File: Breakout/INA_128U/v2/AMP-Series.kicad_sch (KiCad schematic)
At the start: 1 part, among them U1 INA128

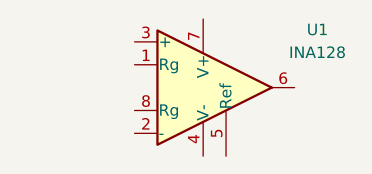
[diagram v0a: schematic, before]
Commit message: added INA128_U v2
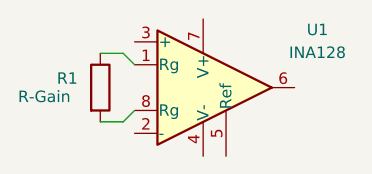
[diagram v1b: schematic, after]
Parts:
- added R1: R-Gain, symbol Device:R
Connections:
- net at U1.1 (Rg): now also R1.1
- net at U1.8 (Rg): now also R1.2
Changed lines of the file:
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@@
 	(generator_version "9.0")
 	(paper "A4")
+	(wire
+		(pts
+			(xy 25.4 43.18) (xy 27.94 43.18)
+		)
+		(stroke
+			(width 0)
+			(type default)
+		)
+	)
+	(wire
+		(pts
+			(xy 25.4 35.56) (xy 27.94 35.56)
+		)
+		(stroke
+			(width 0)
+			(type default)
+		)
+	)
+	(wire
+		(pts
+			(xy 27.94 43.18) (xy 29.21 41.91)
+		)
+		(stroke
+			(width 0)
+			(type default)
+		)
+	)
+	(wire
+		(pts
+			(xy 27.94 35.56) (xy 29.21 36.83)
+		)
+		(stroke
+			(width 0)
+			(type default)
+		)
+	)
+	(symbol
+		(lib_id "Device:R")
+		(at 25.4 39.37 0)
+		(unit 1)
+		(exclude_from_sim no)
+		(in_bom yes)
+		(on_board yes)
+		(dnp no)
+		(property "Reference" "R1"
+			(at 20.574 38.354 0)
+			(effects
+				(font
+					(size 1.27 1.27)
+				)
+				(justify left)
+			)
+		)
+		(property "Value" "R-Gain"
+			(at 16.256 40.386 0)
+			(effects
+				(font
+					(size 1.27 1.27)
+				)
+				(justify left)
+			)
+		)
+		(property "Footprint" ""
+			(at 23.622 39.37 90)
+			(effects
+				(font
+					(size 1.27 1.27)
+				)
+				(hide yes)
+			)
+		)
+		(property "Datasheet" "~"
+			(at 25.4 39.37 0)
+			(effects
+				(font
+					(size 1.27 1.27)
+				)
+				(hide yes)
+			)
+		)
+		(property "Description" "Resistor"
+			(at 25.4 39.37 0)
+			(effects
+				(font
+					(size 1.27 1.27)
+				)
+				(hide yes)
+			)
+		)
+		(pin "1"
+		)
+		(pin "2"
+		)
+		(instances
+			(project ""
+				(path "/59d5f7a4-a278-4e05-9d23-ac911ec59c88"
+					(reference "R1")
+					(unit 1)
+				)
+			)
+		)
+	)
 	(symbol
 		(lib_id "Amplifier_Instrumentation:INA128")
